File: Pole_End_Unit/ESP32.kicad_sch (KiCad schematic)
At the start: 6 parts, among them J4 Conn_01x06_Pin, U3 ESP32-C3-DevKitM-1

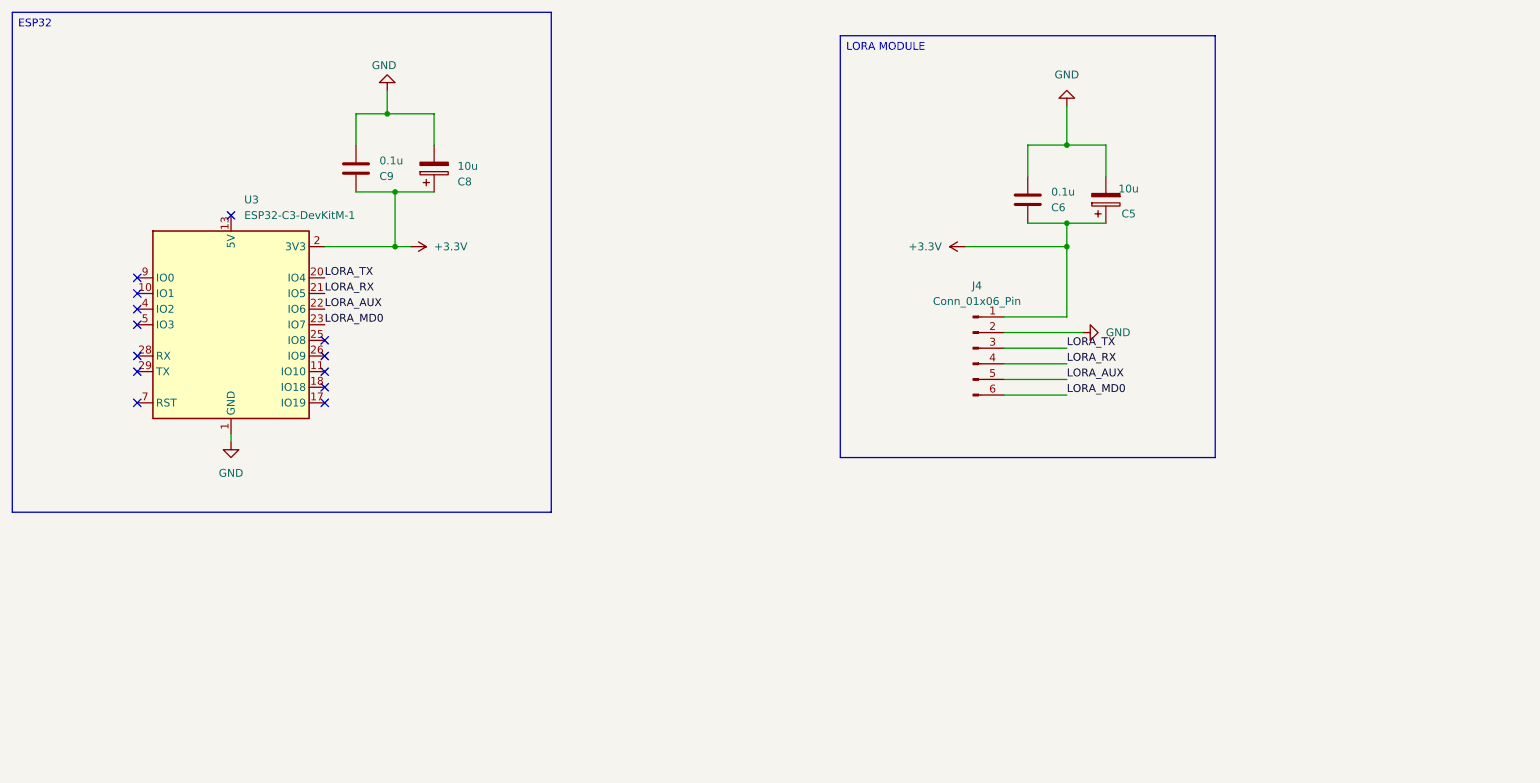
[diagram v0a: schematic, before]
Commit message: Change in the Pole End Unit
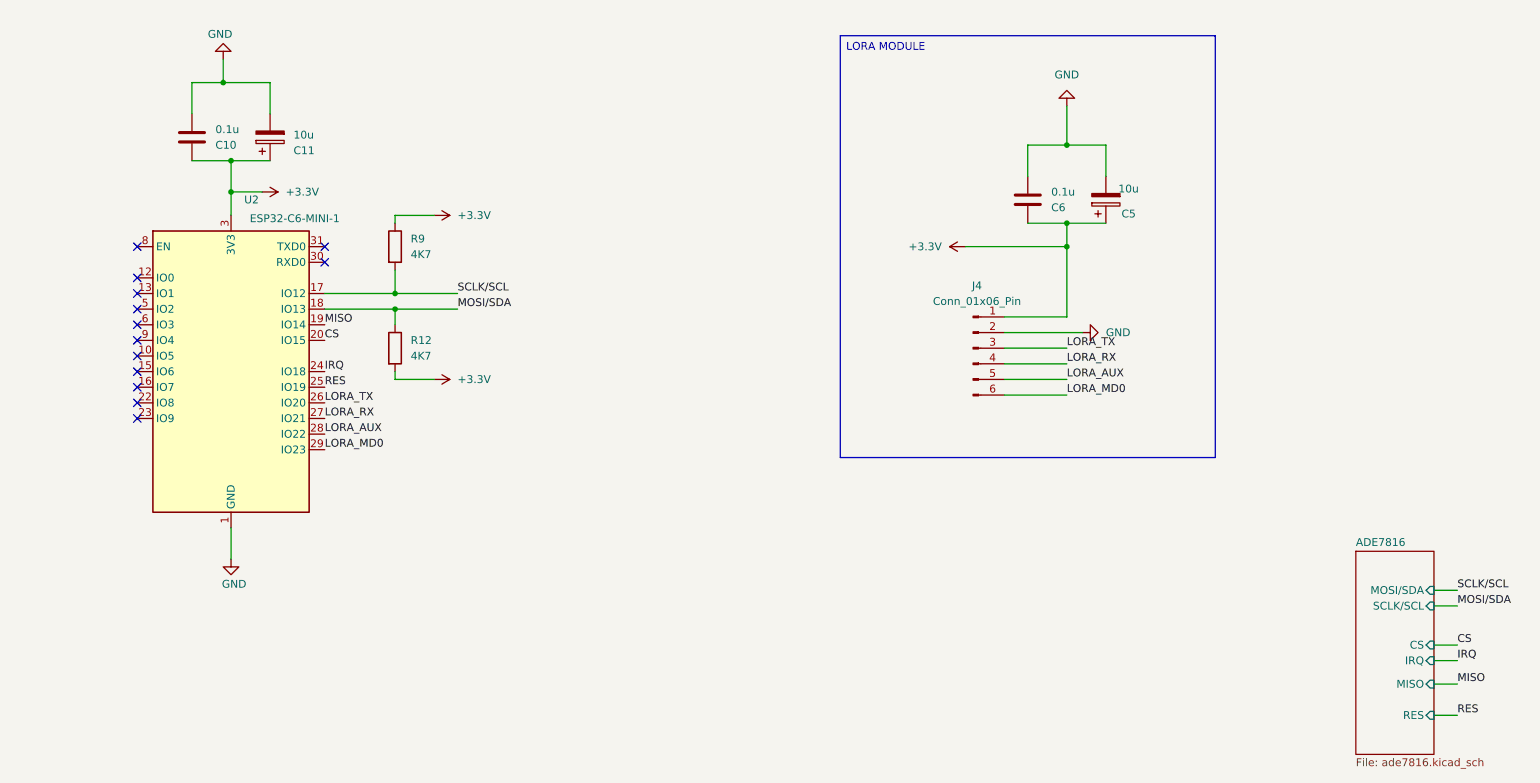
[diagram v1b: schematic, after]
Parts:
- removed C8: 10u, Capacitor_THT:C_Disc_D3.0mm_W1.6mm_P2.50mm, symbol Device:C_Polarized
- removed C9: 0.1u, Capacitor_THT:CP_Radial_D5.0mm_P2.00mm, symbol Device:C
- removed U3: ESP32-C3-DevKitM-1, RF_Module:ESP32-C3-DevKitM-1, symbol RF_Module:ESP32-C3-DevKitM-1
- added C10: 0.1u, Capacitor_SMD:C_0603_1608Metric, symbol Device:C
- added C11: 10u, Capacitor_SMD:C_0603_1608Metric, symbol Device:C_Polarized
- added R12, R9: 4K7, Resistor_SMD:R_0603_1608Metric, symbol Device:R
- added U2: ESP32-C6-MINI-1, RF_Module:ESP32-C6-MINI-1, symbol RF_Module:ESP32-C6-MINI-1
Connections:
- net +3.3V: now also C10.1, C11.1, R12.2, R9.1, U2.3 (3V3)
- net GND: now also C10.2, C11.2, U2.1 (GND), U2.11 (GND), U2.14 (GND), U2.2 (GND), U2.36 (GND), U2.37 (GND), U2.38 (GND), U2.39 (GND), U2.40 (GND), U2.41 (GND), U2.42 (GND), U2.43 (GND), U2.44 (GND), U2.45 (GND), U2.46 (GND), U2.47 (GND), U2.48 (GND), U2.49 (GND), U2.50 (GND), U2.51 (GND), U2.52 (GND), U2.53 (GND)
- net LORA_AUX: now also U2.28 (IO22)
- net LORA_MD0: now also U2.29 (IO23)
- net LORA_RX: now also U2.27 (IO21)
- net LORA_TX: now also U2.26 (IO20)
- new net CS: U2.20 (IO15)
- new net IRQ: U2.24 (IO18)
- new net MISO: U2.19 (IO14)
- new net MOSI/SDA: R12.1, U2.18 (IO13)
- new net RES: U2.25 (IO19)
- new net SCLK/SCL: R9.2, U2.17 (IO12)
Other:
- added sheet ADE7816 (ade7816.kicad_sch)
